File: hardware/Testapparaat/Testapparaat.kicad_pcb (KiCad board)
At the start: 2 copper layers, 138.1 x 142.2 mm, 107 parts, among them J1 IO_SD, J10 B-, J11 Display_shield, J12 GPIO_INPUTS, J13 FrontPanel, J14 GPIO_OUTPUT, J2 Module_1, J3 Module_2, J4 DEBUG, J5 FPC_40P_LCD_ILI9488, J6 IO_UART, J7 Emergency Stop Button, J8 CON-SOCJ-2155, J9 B+, Q1 BC817, Q2 BC817, Q3 BC817, Q4 IRFR9024N, Q5 IRFR9024N, Q6 IRFR9024N, SW1 RST, SW2 on/off switch, U1 74HC595 (SIPO Shift register), U10 LM2596S-5, U11 LM2596S-3.3, U12 74AUC1G74, U2 ESP32-WROOM-32, U4 74HC595 (SIPO Shift register), U5 TCA9534 (IO Expander), U6 74HC14, U7 TCA9534 (IO Expander), U8 74HC14, U9 74HC14

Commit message: -enh drc check
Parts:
- L1, L2: footprint srr1260:SRR1260-680M -> Inductor_SMD:L_Bourns_SRR1260
- moved C19 12.2 mm to (125.5, 37.0), turned to -90 degrees
- moved C20 9.05 mm to (123.8, 37.0), turned to 90 degrees
- moved R13 7.82 mm to (125.3, 59.6), turned to 0 degrees
- moved R12 7.72 mm to (125.3, 58.0), turned to 0 degrees
- moved R11 7.70 mm to (125.3, 56.4), turned to 0 degrees
- moved C18 1.81 mm to (125.1, 54.3), turned to 180 degrees
- moved C9 1.42 mm to (180.0, 130.1)
- moved C22 1.30 mm to (154.6, 36.5)
- moved R32 1.14 mm to (155.4, 43.1)
- moved Q6 1.04 mm to (165.5, 47.3)
- moved C16 0.95 mm to (163.7, 41.2)
- moved D1 0.67 mm to (200.5, 152.2)
- moved D5 0.60 mm to (119.9, 149.3)
- moved R42 0.60 mm to (119.8, 147.6)
- moved R16 0.58 mm to (126.6, 133.1)
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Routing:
- net REG_EN: track 116.7 -> 125.5 mm
- net +3.3V: track 592.6 -> 588.8 mm
- net Net-(J5-Pad36): track 2.31 -> 5.50 mm
- net Net-(J5-Pad35): track 2.68 -> 4.49 mm
- net Net-(Q3-Pad3): track 34.1 -> 35.8 mm
- net +BATT: track 244.6 -> 246.2 mm
- net Net-(Q3-Pad1): track 4.65 -> 5.80 mm
- net Net-(C4-Pad1): track 35.1 -> 35.8 mm

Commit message: -enh drc
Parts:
- moved Q1 1.62 mm to (154.8, 85.9)
- moved Q2 1.48 mm to (160.3, 85.9)
- moved R4 1.47 mm to (157.5, 85.8)
- moved R5 1.00 mm to (157.4, 88.4)
- moved C14 0.78 mm to (134.2, 100.1)
- moved R38 0.41 mm to (147.9, 95.2)
- moved C7 0.39 mm to (115.6, 120.2)
- moved R28 0.30 mm to (115.7, 133.6)
- moved J4 0.20 mm to (158.6, 75.9)
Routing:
- net +BATT: track 246.2 -> 265.2 mm
- net ID_MOD_2: track 92.5 -> 74.6 mm
- net DTR: track 25.2 -> 16.3 mm
- net PWM1_MOD_1: track 78.1 -> 81.1 mm
- net PWM1_MOD_2: track 50.0 -> 51.7 mm
- net RTS: track 3.64 -> 5.09 mm
- net GND: track 199.0 -> 198.0 mm
- net PWM2_MOD_2: track 35.6 -> 36.5 mm, vias 1 -> 3
- net Net-(Q2-Pad1): track 1.47 -> 2.21 mm
- net EMERGENCY_STOP_BTN: track 91.3 -> 92.0 mm
- net TTL2_MOD_2: track 65.0 -> 64.3 mm
- net TTL1_MOD_2: track 66.7 -> 66.0 mm
- net Net-(C7-Pad1): track 12.6 -> 13.2 mm
- net I2C_SCL: track 125.2 -> 125.7 mm
- net TTL3_MOD_1: track 94.0 -> 93.5 mm

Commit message: -enh More drc
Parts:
- moved J14 2.16 mm to (115.3, 105.5)
- moved R19 1.42 mm to (154.2, 96.3)
- moved C1 0.51 mm to (140.3, 62.9)
- moved R20 0.38 mm to (161.6, 55.1)
- moved C17 0.31 mm to (147.4, 99.5)
- moved R43 0.28 mm to (112.2, 112.7)
- moved R1 0.26 mm to (124.2, 98.4)
- moved D5 0.15 mm to (119.8, 149.3)
- moved SW1 0.05 mm to (145.0, 58.4)
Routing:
- net +3.3V: track 589.2 -> 601.0 mm, vias 26 -> 27
- net GPIO_OUTPUT_8: track 10.8 -> 14.7 mm
- net GPIO_OUTPUT_6: track 20.4 -> 23.3 mm
- net GPIO_OUTPUT_7: track 7.03 -> 9.37 mm
- net GPIO_OUTPUT_3: track 12.5 -> 14.8 mm
- net GPIO_OUTPUT_1: track 13.4 -> 15.7 mm
- net GPIO_OUTPUT_2: track 20.1 -> 22.5 mm
- net GPIO_OUTPUT_5: track 31.7 -> 33.6 mm
- net BTN_8: track 33.8 -> 35.5 mm
- net RCLK: track 90.4 -> 88.7 mm
- net GND: track 198.0 -> 199.5 mm
- net EMERGENCY_STOP_BTN: track 92.0 -> 93.4 mm
- net BTN_6: track 32.9 -> 33.9 mm
- net SRCLK: track 88.5 -> 89.5 mm
- net ID_MOD_2: track 74.6 -> 73.6 mm
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
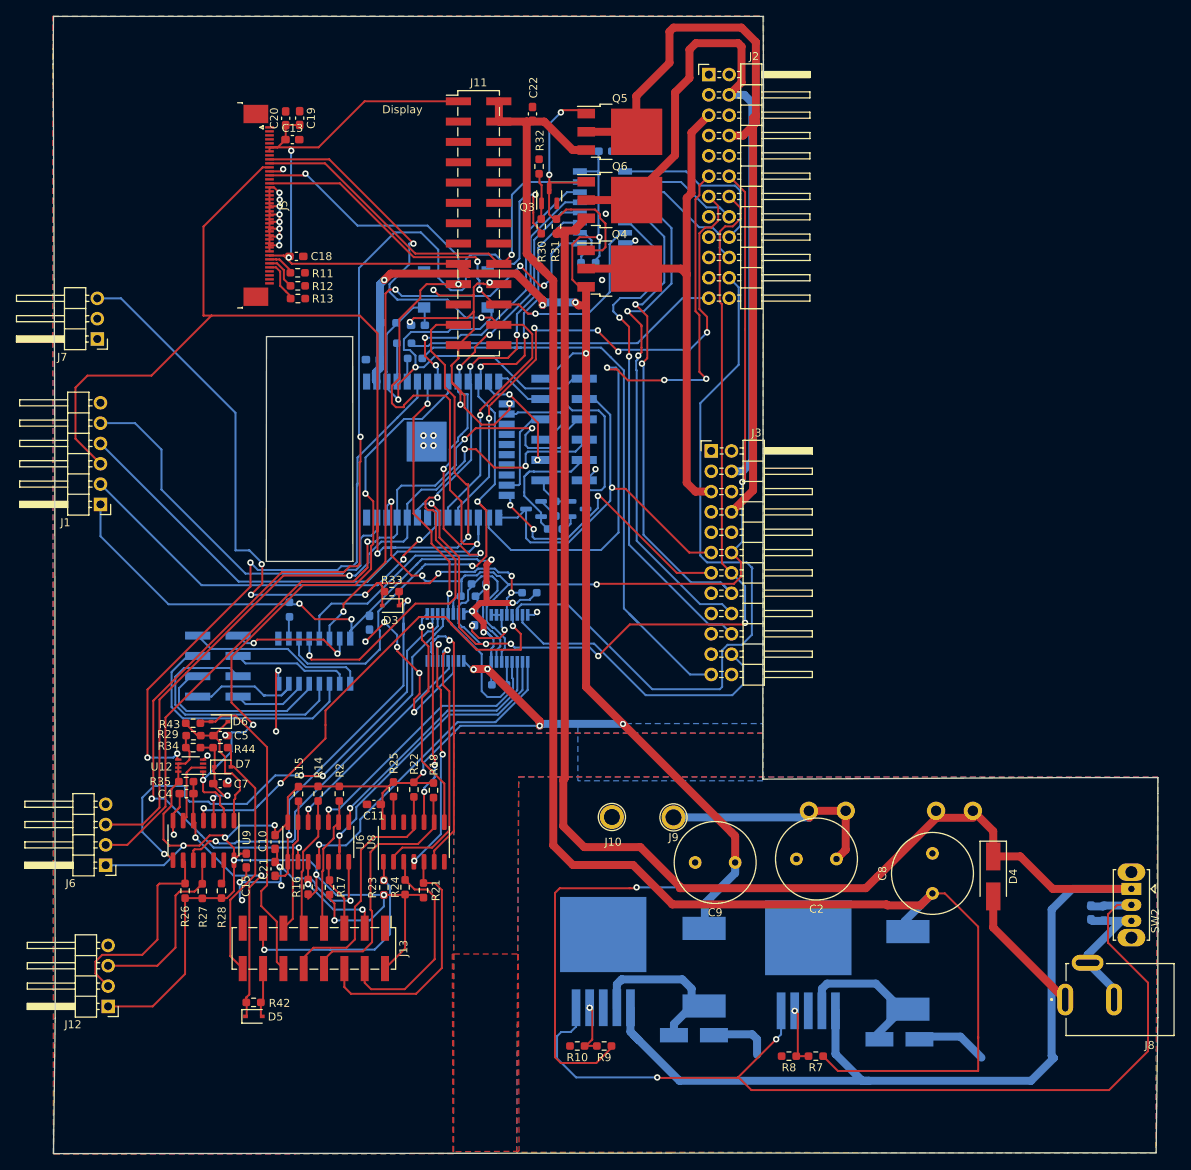
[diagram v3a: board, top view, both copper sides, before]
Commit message: -enh Fixed almost all warnings drc
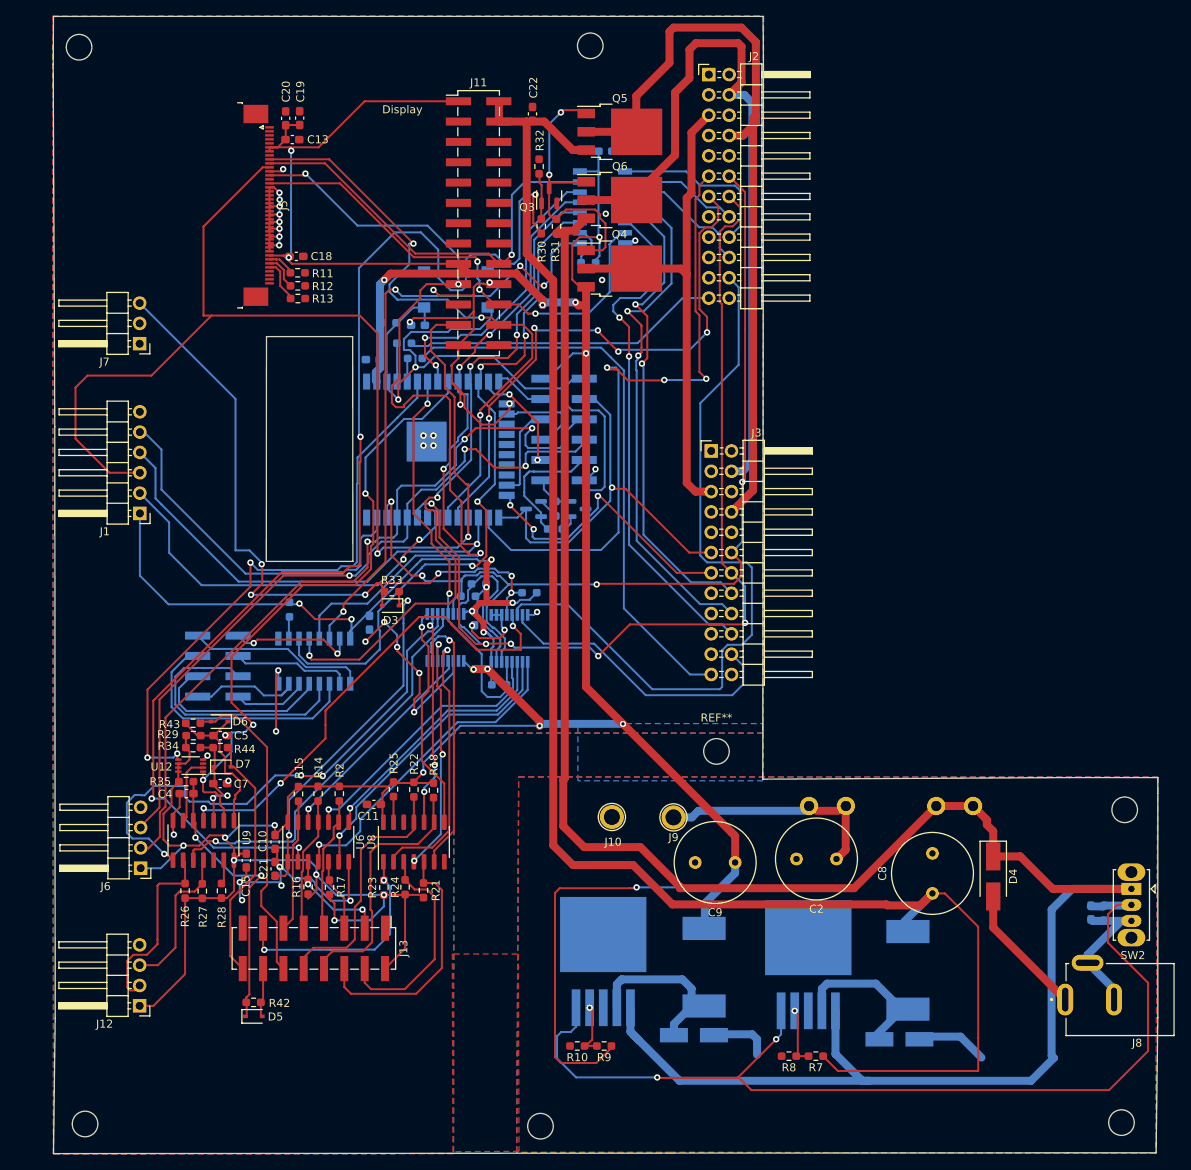
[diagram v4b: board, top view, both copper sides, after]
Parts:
- added ?: , , F.Cu at (97.9, 28.2)
- added ?: , , F.Cu at (155.6, 163.0)
- added ?: , , F.Cu at (228.6, 123.5)
- added ?: , , F.Cu at (161.8, 28.0)
- added ?: , , F.Cu at (228.2, 162.6)
- added ?: , , F.Cu at (98.7, 162.8)
- added REF**: MountingHole_3.2mm_M3, MountingHole:MountingHole_3.2mm_M3, F.Cu at (177.6, 116.2)
- moved J7 5.33 mm to (105.5, 65.2)
- moved J1 5.05 mm to (105.5, 86.4)
- moved J6 4.39 mm to (105.6, 130.8)
- moved J12 3.95 mm to (105.5, 148.0)
- moved F1 0.60 mm to (209.7, 123.0)
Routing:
- net +3.3V: track 601.0 -> 586.4 mm
- net SD_CS: track 51.1 -> 45.7 mm
- net SPI_MOSI: track 142.6 -> 137.3 mm
- net EMERGENCY_STOP_BTN: track 93.4 -> 88.2 mm
- net /MCU/GPIO_3/RXD0: track 94.7 -> 89.9 mm
- net GPIO_INPUT_2_R: track 22.8 -> 18.9 mm
- net GPIO_INPUT_1: track 62.6 -> 66.2 mm
- net SPI_CLK: track 152.4 -> 155.8 mm
- net /MCU/GPIO_1/TXD0: track 100.6 -> 97.3 mm
- net SPI_MISO: track 51.7 -> 48.5 mm
- net Net-(C21-Pad1): track 47.8 -> 45.0 mm
- net ID_MOD_2: track 73.6 -> 71.0 mm
- net RCLK: track 88.7 -> 86.4 mm
- net +5V: track 211.9 -> 209.5 mm
- net Net-(C2-Pad1): track 28.8 -> 26.6 mm
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
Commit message: -add Silkscreen pinouts of headers
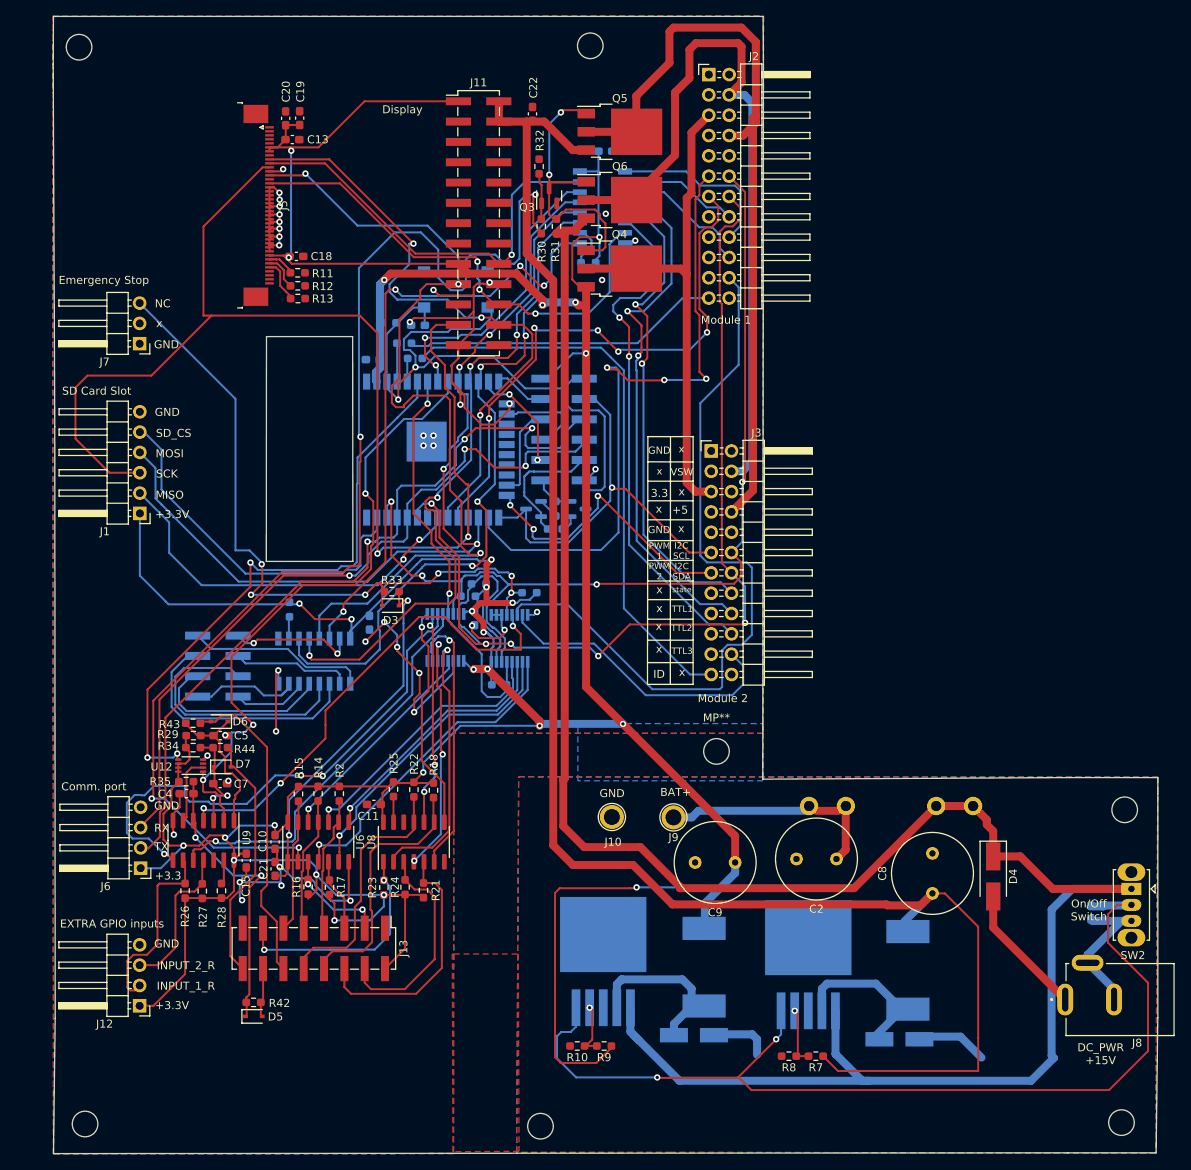
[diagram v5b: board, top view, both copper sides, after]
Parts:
- renumbered REF** to MP**
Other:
- board text added: "+3.3"
- board text added: "+3.3V"
- board text added: "+5"
- board text added: "3.3"
- board text added: "BAT+"
- board text added: "Comm. port"
- board text added: "DC_PWR +15V"
- board text added: "DTR"
- board text added: "EXTRA GPIO inputs"
- board text added: "Emergency Stop"
- board text added: "Extra Output pins"
- board text added: "GND"
- board text added: "I2C SCL"
- board text added: "I2C SDA"
- board text added: "ID"
- board text added: "INPUT_1_R"
- board text added: "INPUT_2_R"
- board text added: "IO2"
- board text added: "MISO"
- board text added: "MOSI"
- board text added: "Module 1"
- board text added: "Module 2"
- board text added: "NC"
- board text added: "OUT1"
- board text added: "OUT2"
- board text added: "OUT3"
- board text added: "OUT4"
- board text added: "OUT5"
- board text added: "OUT6"
- board text added: "OUT7"
- board text added: "OUT8"
- board text added: "On/Off Switch"
- board text added: "PWM 1"
- board text added: "PWM 2"
- board text added: "RST"
- board text added: "RTS"
- board text added: "RX"
- board text added: "RXD"
- board text added: "SCK"
- board text added: "SD Card Slot"
- board text added: "SD_CS"
- board text added: "TCK"
- board text added: "TDI"
- board text added: "TDO"
- board text added: "TMS"
- board text added: "TTL1"
- board text added: "TTL2"
- board text added: "TTL3"
- board text added: "TX"
- board text added: "TXD"
- board text added: "VSW"
- board text added: "state"
- board text added: "x"

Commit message: -add gerbers and minor improvements
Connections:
- J11 pad 26: unconnected-(J11-Pad26) -> Display_TP_CS
- R27 pad 2: GPIO_INPUT_2_R -> Net-(R27-Pad2)
- U7 pad 12: GPIO_INPUT_2 -> Display_TP_CS
- U9 pad 10: GPIO_INPUT_2 -> unconnected-(U9-Pad10)
- U9 pad 11: GPIO_INPUT_2_R -> Net-(R27-Pad2)
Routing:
- net Display_TP_CS: track 0.00 -> 67.2 mm, vias 0 -> 3
- net GPIO_INPUT_2: track 50.5 -> 0.00 mm, vias 1 -> 0
- net GPIO_INPUT_2_R: track 18.9 -> 0.00 mm
- net BTN_7: track 31.7 -> 35.1 mm
- net Net-(R27-Pad2): track 0.00 -> 3.01 mm
- net RCLK: track 86.4 -> 89.1 mm
- net Rotary_BTN: track 60.0 -> 62.7 mm
- net RESET: track 83.1 -> 85.5 mm
- net GND: track 197.7 -> 195.9 mm, vias 41 -> 364
- net SRCLK: track 88.2 -> 89.6 mm
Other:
- outline, holes or cut-outs redrawn
- board text added: "Display (FFC)"
- board text added: "Display (RPI shield)"
- board text added: "Fuse 3A Fast"
- board text added: "Gemaakt door: Jordi Aalbers, Rick van den Brink, Jon Rauwerdink, Ezra den Boer, Teun Rensing, Steven van Ek en Victor Hogeweij"
- board text added: "Hogeschool Arnhem-Nijmegen Project APPS 2022 Main bord"
- board text added: "X"
- board text removed: "Display"
- board text removed: "INPUT_2_R"
